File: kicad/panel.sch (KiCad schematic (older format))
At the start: 7 parts, among them CON21 Panel1, CON22 Panel2, SW1 SW_PUSH, U3 SN74HCT245PW

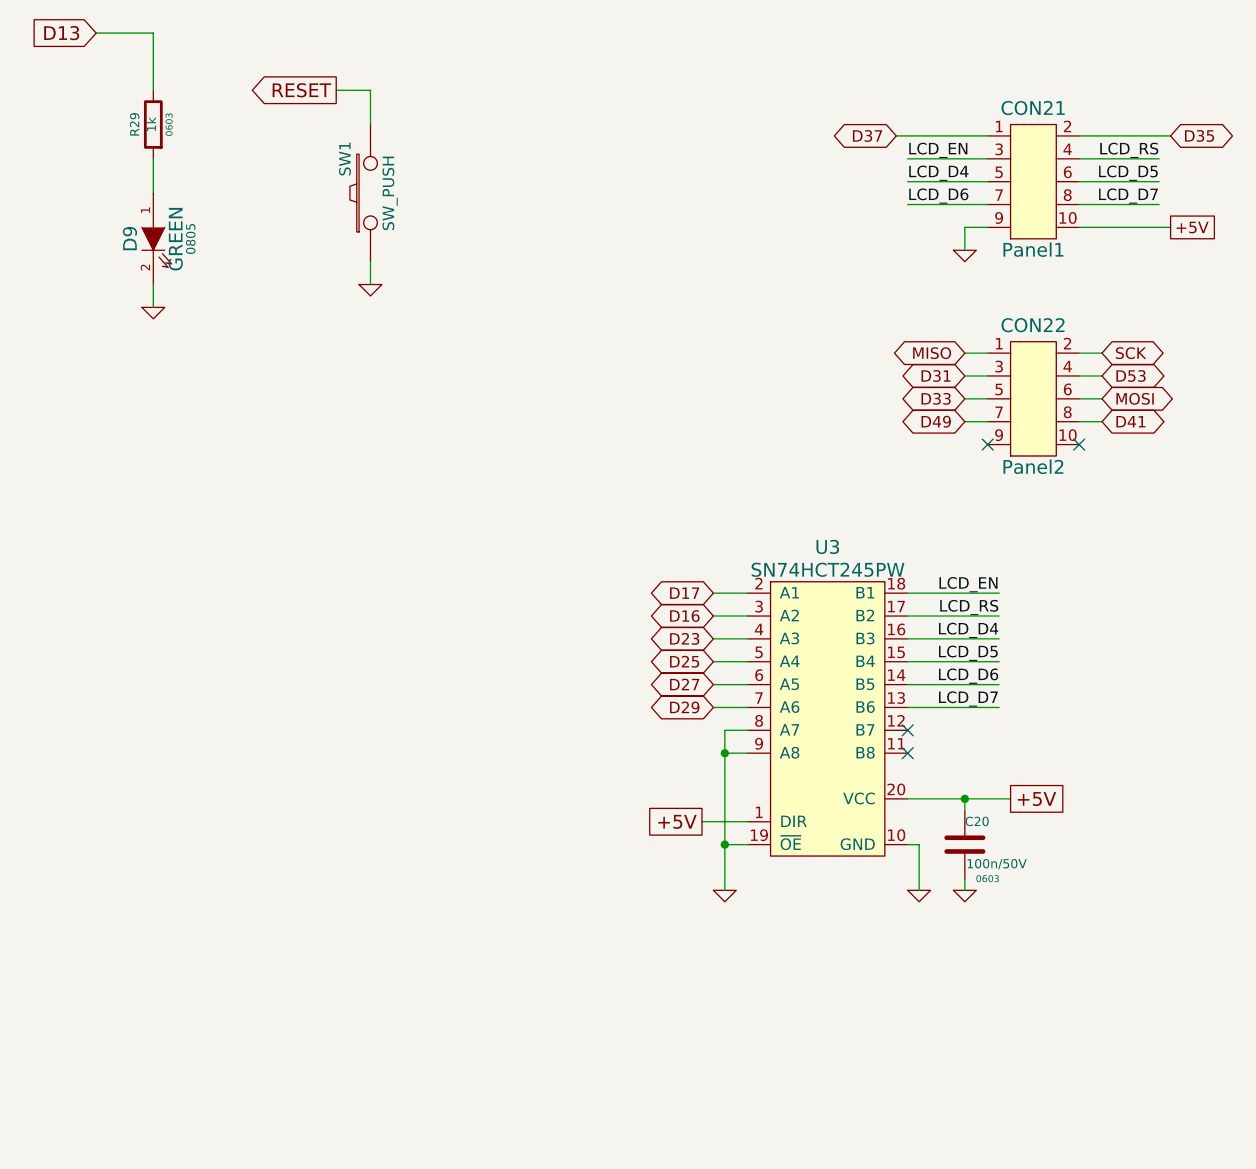
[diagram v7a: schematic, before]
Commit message: Change ULN2803 to discrete MOSFET's FDC6401N
Close #7
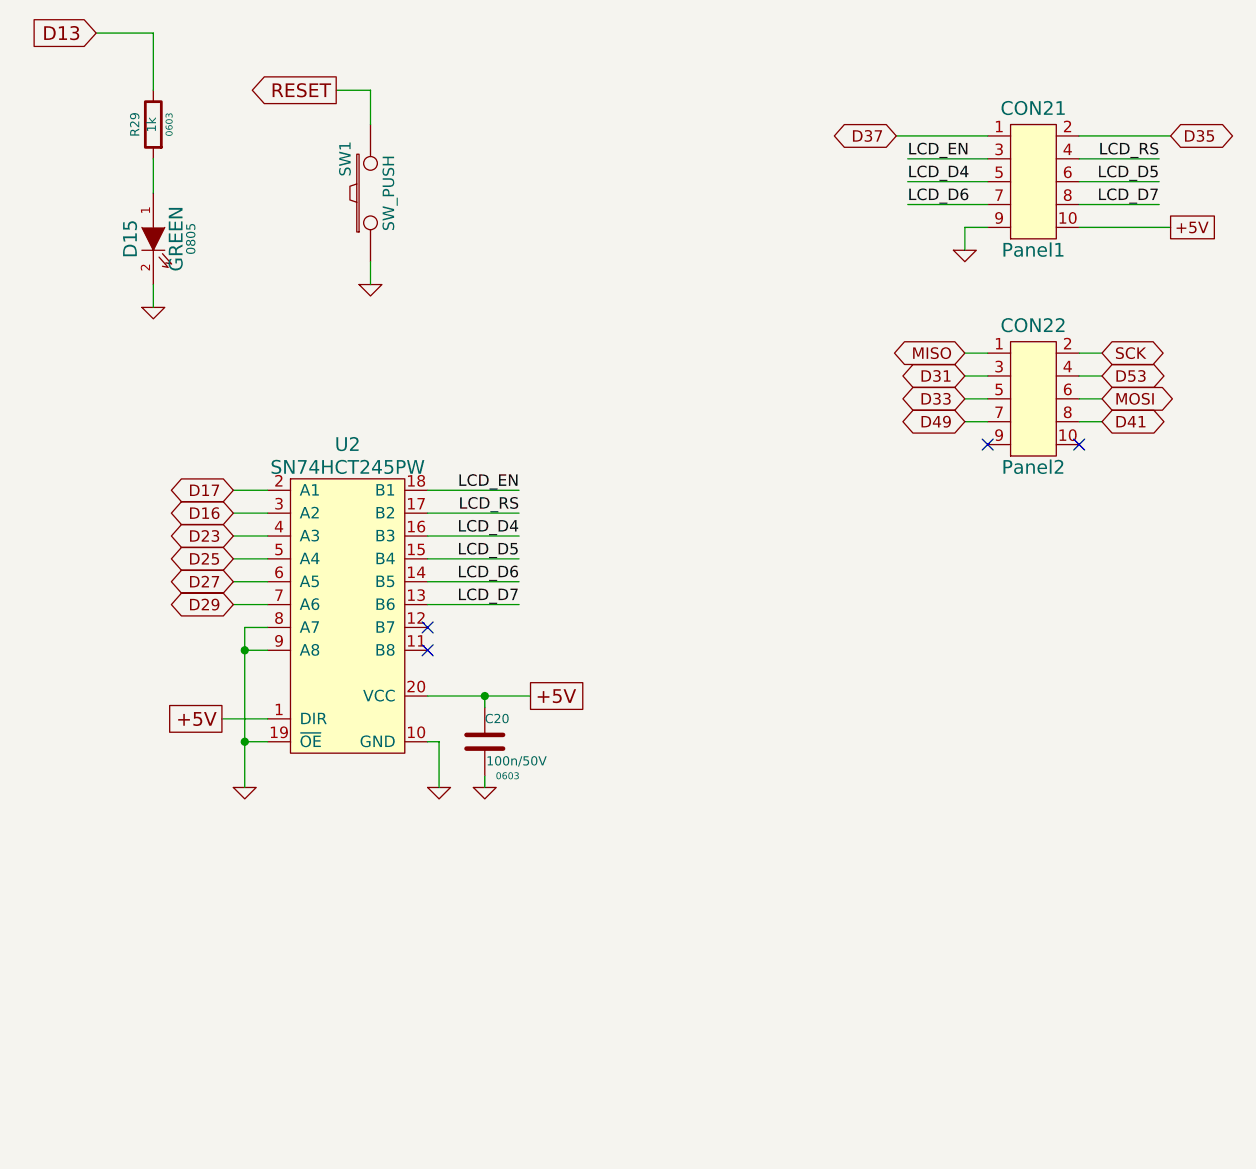
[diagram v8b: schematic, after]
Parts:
- renumbered D9 to D15, U3 to U2
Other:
- moved on the sheet: C20, U2
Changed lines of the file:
@@
 D13
 $Comp
-L GND #PWR54
+L GND #PWR064
 U 1 1 534EE36C
 P 2000 2250
-F 0 "#PWR54" H 2000 2250 30  0001 C CNN
+F 0 "#PWR064" H 2000 2250 30  0001 C CNN
 F 1 "GND" H 2000 2180 30  0001 C CNN
 F 2 "~" H 2000 2250 60  0000 C CNN
@@
 $EndComp
 $Comp
-L GND #PWR53
+L GND #PWR065
 U 1 1 536AA50B
 P 2950 2150
-F 0 "#PWR53" H 2950 2150 30  0001 C CNN
+F 0 "#PWR065" H 2950 2150 30  0001 C CNN
 F 1 "GND" H 2950 2080 30  0001 C CNN
 F 2 "~" H 2950 2150 60  0000 C CNN
@@
 RESET
 $Comp
-L LED D9
+L LED D15
 U 1 1 536FE241
 P 2000 1950
-F 0 "D9" H 2000 2050 60  0000 C CNN
+F 0 "D15" H 2000 2050 60  0000 C CNN
 F 1 "GREEN" H 2000 1850 60  0000 C CNN
 F 2 "0805" H 2000 1785 40  0000 C CNN
@@
 	1    0    0    -1
 $EndComp
-Text GLabel 4450 3500 0    50   BiDi ~ 0
+Text GLabel 2350 3050 0    50   BiDi ~ 0
 D17
-Text GLabel 4450 3700 0    50   BiDi ~ 0
+Text GLabel 2350 3250 0    50   BiDi ~ 0
 D23
-Text GLabel 4450 3900 0    50   BiDi ~ 0
+Text GLabel 2350 3450 0    50   BiDi ~ 0
 D27
-Text GLabel 4450 3600 0    50   BiDi ~ 0
+Text GLabel 2350 3150 0    50   BiDi ~ 0
 D16
-Text GLabel 4450 3800 0    50   BiDi ~ 0
+Text GLabel 2350 3350 0    50   BiDi ~ 0
 D25
-Text GLabel 4450 4000 0    50   BiDi ~ 0
+Text GLabel 2350 3550 0    50   BiDi ~ 0
 D29
 Wire Wire Line
@@
 	5650 1500 5250 1500
 $Comp
-L GND #PWR52
+L GND #PWR066
 U 1 1 538CDD99
 P 5550 2000
-F 0 "#PWR52" H 5550 2000 30  0001 C CNN
+F 0 "#PWR066" H 5550 2000 30  0001 C CNN
 F 1 "GND" H 5550 1930 30  0001 C CNN
 F 2 "~" H 5550 2000 60  0000 C CNN
@@
 D49
 $Comp
-L SN74HCT245PW U3
+L SN74HCT245PW U2
 U 1 1 538E2F48
-P 4950 3850
-F 0 "U3" H 4950 4400 60  0000 C CNN
-F 1 "SN74HCT245PW" H 4950 4300 60  0000 C CNN
-F 2 "" H 4950 4350 60  0000 C CNN
-F 3 "" H 4950 4350 60  0000 C CNN
-	1    4950 3850
+P 2850 3400
+F 0 "U2" H 2850 3950 60  0000 C CNN
+F 1 "SN74HCT245PW" H 2850 3850 60  0000 C CNN
+F 2 "" H 2850 3900 60  0000 C CNN
+F 3 "" H 2850 3900 60  0000 C CNN
+	1    2850 3400
 	1    0    0    -1
 $EndComp
@@
 L C C20
 U 1 1 538E32B7
-P 5550 4600
-F 0 "C20" H 5550 4700 40  0000 L CNN
-F 1 "100n/50V" H 5556 4515 40  0000 L CNN
-F 2 "0603" H 5650 4450 30  0000 C CNN
-F 3 "" H 5550 4600 60  0000 C CNN
-	1    5550 4600
-	1    0    0    -1
-$EndComp
-$Comp
-L GND #PWR57
+P 3450 4150
+F 0 "C20" H 3450 4250 40  0000 L CNN
+F 1 "100n/50V" H 3456 4065 40  0000 L CNN
+F 2 "0603" H 3550 4000 30  0000 C CNN
+F 3 "" H 3450 4150 60  0000 C CNN
+	1    3450 4150
+	1    0    0    -1
+$EndComp
+$Comp
+L GND #PWR067
 U 1 1 538E32BE
-P 5550 4800
-F 0 "#PWR57" H 5550 4800 30  0001 C CNN
-F 1 "GND" H 5550 4730 30  0001 C CNN
-F 2 "" H 5550 4800 60  0000 C CNN
-F 3 "" H 5550 4800 60  0000 C CNN
-	1    5550 4800
-	1    0    0    -1
-$EndComp
-Wire Wire Line
-	5550 4400 5550 4450
-Wire Wire Line
-	5550 4750 5550 4800
-Wire Wire Line
-	5300 4400 5750 4400
-$Comp
-L GND #PWR56
+P 3450 4350
+F 0 "#PWR067" H 3450 4350 30  0001 C CNN
+F 1 "GND" H 3450 4280 30  0001 C CNN
+F 2 "" H 3450 4350 60  0000 C CNN
+F 3 "" H 3450 4350 60  0000 C CNN
+	1    3450 4350
+	1    0    0    -1
+$EndComp
+Wire Wire Line
+	3450 3950 3450 4000
+Wire Wire Line
+	3450 4300 3450 4350
+Wire Wire Line
+	3200 3950 3650 3950
+$Comp
+L GND #PWR068
 U 1 1 538E3349
-P 5350 4800
-F 0 "#PWR56" H 5350 4800 30  0001 C CNN
-F 1 "GND" H 5350 4730 30  0001 C CNN
-F 2 "" H 5350 4800 60  0000 C CNN
-F 3 "" H 5350 4800 60  0000 C CNN
-	1    5350 4800
-	1    0    0    -1
-$EndComp
-Wire Wire Line
-	5350 4800 5350 4600
-Wire Wire Line
-	5350 4600 5300 4600
-Text GLabel 5750 4400 2    60   UnSpc ~ 0
+P 3250 4350
+F 0 "#PWR068" H 3250 4350 30  0001 C CNN
+F 1 "GND" H 3250 4280 30  0001 C CNN
+F 2 "" H 3250 4350 60  0000 C CNN
+F 3 "" H 3250 4350 60  0000 C CNN
+	1    3250 4350
+	1    0    0    -1
+$EndComp
+Wire Wire Line
+	3250 4350 3250 4150
+Wire Wire Line
+	3250 4150 3200 4150
+Text GLabel 3650 3950 2    60   UnSpc ~ 0
 +5V
-Connection ~ 5550 4400
-Text GLabel 4400 4500 0    60   UnSpc ~ 0
+Connection ~ 3450 3950
+Text GLabel 2300 4050 0    60   UnSpc ~ 0
 +5V
 Wire Wire Line
-	4600 4500 4400 4500
-$Comp
-L GND #PWR55
+	2500 4050 2300 4050
+$Comp
+L GND #PWR069
 U 1 1 538E301C
-P 4500 4800
-F 0 "#PWR55" H 4500 4800 30  0001 C CNN
-F 1 "GND" H 4500 4730 30  0001 C CNN
-F 2 "" H 4500 4800 60  0000 C CNN
-F 3 "" H 4500 4800 60  0000 C CNN
-	1    4500 4800
-	1    0    0    -1
-$EndComp
-Wire Wire Line
-	4500 4100 4500 4800
-Wire Wire Line
-	4500 4600 4600 4600
-Wire Wire Line
-	4450 3500 4600 3500
-Wire Wire Line
-	4450 3600 4600 3600
-Wire Wire Line
-	4450 3700 4600 3700
-Wire Wire Line
-	4450 3800 4600 3800
-Wire Wire Line
-	4450 3900 4600 3900
-Wire Wire Line
-	4450 4000 4600 4000
+P 2400 4350
+F 0 "#PWR069" H 2400 4350 30  0001 C CNN
+F 1 "GND" H 2400 4280 30  0001 C CNN
+F 2 "" H 2400 4350 60  0000 C CNN
+F 3 "" H 2400 4350 60  0000 C CNN
+	1    2400 4350
+	1    0    0    -1
+$EndComp
+Wire Wire Line
+	2400 3650 2400 4350
+Wire Wire Line
+	2400 4150 2500 4150
+Wire Wire Line
+	2350 3050 2500 3050
+Wire Wire Line
+	2350 3150 2500 3150
+Wire Wire Line
+	2350 3250 2500 3250
+Wire Wire Line
+	2350 3350 2500 3350
+Wire Wire Line
+	2350 3450 2500 3450
+Wire Wire Line
+	2350 3550 2500 3550
 Text Label 5300 1600 0    50   ~ 0
 LCD_EN
@@
 Text Label 6400 1800 2    50   ~ 0
 LCD_D7
-Text Label 5700 3500 2    50   ~ 0
+Text Label 3600 3050 2    50   ~ 0
 LCD_EN
-Text Label 5700 3700 2    50   ~ 0
+Text Label 3600 3250 2    50   ~ 0
 LCD_D4
-Text Label 5700 3900 2    50   ~ 0
+Text Label 3600 3450 2    50   ~ 0
 LCD_D6
-Text Label 5700 3600 2    50   ~ 0
+Text Label 3600 3150 2    50   ~ 0
 LCD_RS
-Text Label 5700 3800 2    50   ~ 0
+Text Label 3600 3350 2    50   ~ 0
 LCD_D5
-Text Label 5700 4000 2    50   ~ 0
+Text Label 3600 3550 2    50   ~ 0
 LCD_D7
 Wire Wire Line
-	5300 3500 5700 3500
-Wire Wire Line
-	5700 3600 5300 3600
-Wire Wire Line
-	5300 3700 5700 3700
-Wire Wire Line
-	5700 3800 5300 3800
-Wire Wire Line
-	5300 3900 5700 3900
-Wire Wire Line
-	5700 4000 5300 4000
-Wire Wire Line
-	4600 4100 4500 4100
-Connection ~ 4500 4600
-Wire Wire Line
-	4600 4200 4500 4200
-Connection ~ 4500 4200
-NoConn ~ 5300 4100
-NoConn ~ 5300 4200
+	3200 3050 3600 3050
+Wire Wire Line
+	3600 3150 3200 3150
+Wire Wire Line
+	3200 3250 3600 3250
+Wire Wire Line
+	3600 3350 3200 3350
+Wire Wire Line
+	3200 3450 3600 3450
+Wire Wire Line
+	3600 3550 3200 3550
+Wire Wire Line
+	2500 3650 2400 3650
+Connection ~ 2400 4150
+Wire Wire Line
+	2500 3750 2400 3750
+Connection ~ 2400 3750
+NoConn ~ 3200 3650
+NoConn ~ 3200 3750
 $EndSCHEMATC
